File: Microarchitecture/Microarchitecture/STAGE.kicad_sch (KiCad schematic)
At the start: 4 parts

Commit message: Updated timing diagrams, etc, control fsm and verified workings
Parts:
- removed MUX4: ~, symbol Symbols:MUX_BUS
- added MUX2: ~, symbol Symbols:MUX_BUS
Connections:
- net BLAKELEY_MODULE1/A is gone; now on net PREG_RST: REG1. (RST)
- net BLAKELEY_MODULE1/B is gone; now on net DCO: REG8. (RST)
- net BLAKELEY_MODULE1/R: now also MUX1. (MUX[W-1...0])
- net BLAKELEY_MODULE2/R: now also MUX2. (MUX[W-1...0]); no longer MUX1.2 (M1[W-1...0])
- net CMUX_C0: now also MUX1. (MUX[W-1...0])
- net DCI: now also MUX1. (MUX[W-1...0])
- net DPI: now also MUX2. (MUX[W-1...0]); no longer MUX1.1 (M0[W-1...0])
- net DPO: now also REG1. (RST)
- net PMUX_C0: now also MUX2. (MUX[W-1...0]); no longer MUX1.4 (C0)
- new net: MUX2. (MUX[W-1...0]), REG1. (RST)
- new net: MUX1. (MUX[W-1...0]), REG8. (RST)
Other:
- note added: "From rsa_regio"
- note removed: "From upper level"
- moved on the sheet: REG1, REG8

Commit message: Latest changes
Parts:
- renumbered MUX2 to MUX10, MUX1 to MUX9, REG8 to REG16, REG1 to REG17
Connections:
- new net: MUX10. (MUX[W-1...0]), REG17. (RST)
- new net: MUX9. (MUX[W-1...0]), REG16. (RST)
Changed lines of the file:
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@@
 	(wire
 		(pts
-			(xy 302.26 21.59) (xy 302.26 34.29)
+			(xy 307.34 38.1) (xy 307.34 50.8)
 		)
 		(stroke
@@
 	(wire
 		(pts
-			(xy 381 119.38) (xy 396.24 119.38)
+			(xy 374.65 118.11) (xy 389.89 118.11)
 		)
 		(stroke
@@
 	(wire
 		(pts
-			(xy 381 106.68) (xy 396.24 106.68)
+			(xy 374.65 105.41) (xy 389.89 105.41)
 		)
 		(stroke
@@
 	(wire
 		(pts
-			(xy 212.09 115.57) (xy 196.85 115.57)
+			(xy 218.44 115.57) (xy 203.2 115.57)
 		)
 		(stroke
@@
 	(polyline
 		(pts
-			(xy 391.16 95.25) (xy 391.16 127)
+			(xy 384.81 93.98) (xy 384.81 125.73)
 		)
 		(stroke
@@
 	(wire
 		(pts
-			(xy 294.64 21.59) (xy 294.64 34.29)
+			(xy 299.72 38.1) (xy 299.72 50.8)
 		)
 		(stroke
@@
 	(polyline
 		(pts
-			(xy 284.48 26.67) (xy 311.15 26.67)
+			(xy 289.56 43.18) (xy 316.23 43.18)
 		)
 		(stroke
@@
 	(polyline
 		(pts
-			(xy 201.93 93.98) (xy 201.93 125.73)
+			(xy 208.28 93.98) (xy 208.28 125.73)
 		)
 		(stroke
@@
 	(wire
 		(pts
-			(xy 212.09 118.11) (xy 196.85 118.11)
+			(xy 218.44 118.11) (xy 203.2 118.11)
 		)
 		(stroke
@@
 	(wire
 		(pts
-			(xy 381 102.87) (xy 396.24 102.87)
+			(xy 374.65 101.6) (xy 389.89 101.6)
 		)
 		(stroke
@@
 	(wire
 		(pts
-			(xy 212.09 105.41) (xy 196.85 105.41)
+			(xy 218.44 105.41) (xy 203.2 105.41)
 		)
 		(stroke
@@
 	(wire
 		(pts
-			(xy 212.09 101.6) (xy 196.85 101.6)
+			(xy 218.44 101.6) (xy 203.2 101.6)
 		)
 		(stroke
@@
 	(wire
 		(pts
-			(xy 381 116.84) (xy 396.24 116.84)
+			(xy 374.65 115.57) (xy 389.89 115.57)
 		)
 		(stroke
@@
 	)
 	(image
-		(at 144.78 243.84)
-		(scale 0.606573)
+		(at 99.06 242.57)
+		(scale 0.211169)
 		(data "iVBORw0KGgoAAAANSUhEUgAACVEAAAK8CAYAAADsh23GAAAAAXNSR0IArs4c6QAAAARnQU1BAACx"
 			"jwv8YQUAAAAJcEhZcwAAFiUAABYlAUlSJPAAAP+lSURBVHhe7P0PbFT3ne//v20mLNT1jrG/tKak"
@@
 	(text "From rsa_regio"
 		(exclude_from_sim no)
-		(at 282.448 23.368 0)
+		(at 287.528 39.878 0)
 		(effects
 			(font
@@
 	(text "To/From previous stage"
 		(exclude_from_sim no)
-		(at 203.708 91.694 0)
+		(at 210.058 91.694 0)
 		(effects
 			(font
@@
 	(text "To/From next stage"
 		(exclude_from_sim no)
-		(at 390.144 94.234 0)
+		(at 383.794 92.964 0)
 		(effects
 			(font
@@
 	)
 	(label "DCI"
-		(at 212.09 105.41 0)
+		(at 218.44 105.41 0)
 		(fields_autoplaced yes)
 		(effects
@@
 	)
 	(label "ES"
-		(at 302.26 34.29 180)
+		(at 307.34 50.8 180)
 		(fields_autoplaced yes)
 		(effects
@@
 	)
 	(label "IPI"
-		(at 381 116.84 180)
+		(at 374.65 115.57 180)
 		(fields_autoplaced yes)
 		(effects
@@
 	)
 	(label "DPI"
-		(at 212.09 101.6 0)
+		(at 218.44 101.6 0)
 		(fields_autoplaced yes)
 		(effects
@@
 	)
 	(label "DCO"
-		(at 381 106.68 180)
+		(at 374.65 105.41 180)
 		(fields_autoplaced yes)
 		(effects
@@
 	)
 	(label "DPO"
-		(at 381 102.87 180)
+		(at 374.65 101.6 180)
 		(fields_autoplaced yes)
 		(effects
@@
 	)
 	(label "ILO"
-		(at 381 119.38 180)
+		(at 374.65 118.11 180)
 		(fields_autoplaced yes)
 		(effects
@@
 	)
 	(label "ILI"
-		(at 212.09 115.57 0)
+		(at 218.44 115.57 0)
 		(fields_autoplaced yes)
 		(effects
@@
 	)
 	(label "N"
-		(at 294.64 34.29 180)
+		(at 299.72 50.8 180)
 		(fields_autoplaced yes)
 		(effects
@@
 	)
 	(label "IPO"
-		(at 212.09 118.11 0)
+		(at 218.44 118.11 0)
 		(fields_autoplaced yes)
 		(effects
@@
 	(hierarchical_label "ILO"
 		(shape output)
-		(at 396.24 119.38 0)
+		(at 389.89 118.11 0)
 		(fields_autoplaced yes)
 		(effects
@@
 	(hierarchical_label "IPO"
 		(shape output)
-		(at 196.85 118.11 180)
+		(at 203.2 118.11 180)
 		(fields_autoplaced yes)
 		(effects
@@
 	(hierarchical_label "N"
 		(shape input)
-		(at 294.64 21.59 90)
+		(at 299.72 38.1 90)
 		(fields_autoplaced yes)
 		(effects
@@
 	(hierarchical_label "DCO"
 		(shape output)
-		(at 396.24 106.68 0)
+		(at 389.89 105.41 0)
 		(fields_autoplaced yes)
 		(effects
@@
 	(hierarchical_label "IPI"
 		(shape input)
-		(at 396.24 116.84 0)
+		(at 389.89 115.57 0)
 		(fields_autoplaced yes)
 		(effects
@@
 		)
 		(property "Netclass" ""
-			(at 396.24 118.11 0)
+			(at 389.89 116.84 0)
 			(effects
 				(font
@@
 	(hierarchical_label "DCI"
 		(shape input)
-		(at 196.85 105.41 180)
+		(at 203.2 105.41 180)
 		(fields_autoplaced yes)
 		(effects
@@
 	(hierarchical_label "ILI"
 		(shape input)
-		(at 196.85 115.57 180)
+		(at 203.2 115.57 180)
 		(fields_autoplaced yes)
 		(effects
@@
 	(hierarchical_label "ES"
 		(shape input)
-		(at 302.26 21.59 90)
+		(at 307.34 38.1 90)
 		(fields_autoplaced yes)
 		(effects
@@
 	(hierarchical_label "DPI"
 		(shape input)
-		(at 196.85 101.6 180)
+		(at 203.2 101.6 180)
 		(fields_autoplaced yes)
 		(effects
@@
 	(hierarchical_label "DPO"
 		(shape output)
-		(at 396.24 102.87 0)
+		(at 389.89 101.6 0)
 		(fields_autoplaced yes)
 		(effects
@@
 		(on_board yes)
 		(dnp no)
-		(property "Reference" "MUX2"
+		(property "Reference" "MUX10"
 			(at 247.904 137.16 0)
 			(effects
@@
 		)
 		(instances
-			(project ""
-				(path "/7e18b03f-0dd8-4430-9873-65919f4f0c9c/21c2d8ae-34c8-4eeb-a025-0344b2d7e18d/d24df161-92da-4d3c-8ec4-b2b340dd12b4"
-					(reference "MUX2")
+			(project "Microarchitecture"
+				(path "/7e18b03f-0dd8-4430-9873-65919f4f0c9c/21c2d8ae-34c8-4eeb-a025-0344b2d7e18d/2ff9fb5f-e895-4ed8-9926-01fc2395a11b"
+					(reference "MUX10")
+					(unit 1)
+				)
+				(path "/7e18b03f-0dd8-4430-9873-65919f4f0c9c/21c2d8ae-34c8-4eeb-a025-0344b2d7e18d/5c7540d9-7028-48a5-955b-0e835a2154cd"
+					(reference "MUX5")
 					(unit 1)
 				)
@@
 	)
 	(symbol
-		(lib_name "Symbols:REG")
 		(lib_id "Symbols:REG")
 		(at 313.69 66.04 0)
@@
 		(on_board yes)
 		(dnp no)
-		(property "Reference" "REG8"
+		(property "Reference" "REG16"
 			(at 319.786 57.658 0)
 			(effects
@@
 		(instances
 			(project "Microarchitecture"
+				(path "/7e18b03f-0dd8-4430-9873-65919f4f0c9c/21c2d8ae-34c8-4eeb-a025-0344b2d7e18d/2ff9fb5f-e895-4ed8-9926-01fc2395a11b"
+					(reference "REG16")
+					(unit 1)
+				)
+				(path "/7e18b03f-0dd8-4430-9873-65919f4f0c9c/21c2d8ae-34c8-4eeb-a025-0344b2d7e18d/5c7540d9-7028-48a5-955b-0e835a2154cd"
+					(reference "REG4")
+					(unit 1)
+				)
 				(path "/7e18b03f-0dd8-4430-9873-65919f4f0c9c/21c2d8ae-34c8-4eeb-a025-0344b2d7e18d/d24df161-92da-4d3c-8ec4-b2b340dd12b4"
 					(reference "REG8")
@@
 	)
 	(symbol
-		(lib_name "Symbols:REG")
 		(lib_id "Symbols:REG")
 		(at 313.69 152.4 0)
@@
 		(on_board yes)
 		(dnp no)
-		(property "Reference" "REG1"
+		(property "Reference" "REG17"
 			(at 319.786 144.018 0)
 			(effects
@@
 		(instances
 			(project "Microarchitecture"
+				(path "/7e18b03f-0dd8-4430-9873-65919f4f0c9c/21c2d8ae-34c8-4eeb-a025-0344b2d7e18d/2ff9fb5f-e895-4ed8-9926-01fc2395a11b"
+					(reference "REG17")
+					(unit 1)
+				)
+				(path "/7e18b03f-0dd8-4430-9873-65919f4f0c9c/21c2d8ae-34c8-4eeb-a025-0344b2d7e18d/5c7540d9-7028-48a5-955b-0e835a2154cd"
+					(reference "REG6")
+					(unit 1)
+				)
 				(path "/7e18b03f-0dd8-4430-9873-65919f4f0c9c/21c2d8ae-34c8-4eeb-a025-0344b2d7e18d/d24df161-92da-4d3c-8ec4-b2b340dd12b4"
 					(reference "REG1")
@@
 		(on_board yes)
 		(dnp no)
-		(property "Reference" "MUX1"
+		(property "Reference" "MUX9"
 			(at 247.904 50.8 0)
 			(effects
@@
 		(instances
 			(project "Microarchitecture"
+				(path "/7e18b03f-0dd8-4430-9873-65919f4f0c9c/21c2d8ae-34c8-4eeb-a025-0344b2d7e18d/2ff9fb5f-e895-4ed8-9926-01fc2395a11b"
+					(reference "MUX9")
+					(unit 1)
+				)
+				(path "/7e18b03f-0dd8-4430-9873-65919f4f0c9c/21c2d8ae-34c8-4eeb-a025-0344b2d7e18d/5c7540d9-7028-48a5-955b-0e835a2154cd"
+					(reference "MUX4")
+					(unit 1)
+				)
 				(path "/7e18b03f-0dd8-4430-9873-65919f4f0c9c/21c2d8ae-34c8-4eeb-a025-0344b2d7e18d/d24df161-92da-4d3c-8ec4-b2b340dd12b4"
 					(reference "MUX1")
@@
 					(page "6")
 				)
+				(path "/7e18b03f-0dd8-4430-9873-65919f4f0c9c/21c2d8ae-34c8-4eeb-a025-0344b2d7e18d/5c7540d9-7028-48a5-955b-0e835a2154cd"
+					(page "10")
+				)
+				(path "/7e18b03f-0dd8-4430-9873-65919f4f0c9c/21c2d8ae-34c8-4eeb-a025-0344b2d7e18d/2ff9fb5f-e895-4ed8-9926-01fc2395a11b"
+					(page "13")
+				)
 			)
 		)
@@
 					(page "5")
 				)
+				(path "/7e18b03f-0dd8-4430-9873-65919f4f0c9c/21c2d8ae-34c8-4eeb-a025-0344b2d7e18d/5c7540d9-7028-48a5-955b-0e835a2154cd"
+					(page "11")
+				)
+				(path "/7e18b03f-0dd8-4430-9873-65919f4f0c9c/21c2d8ae-34c8-4eeb-a025-0344b2d7e18d/2ff9fb5f-e895-4ed8-9926-01fc2395a11b"
+					(page "14")
+				)
 			)

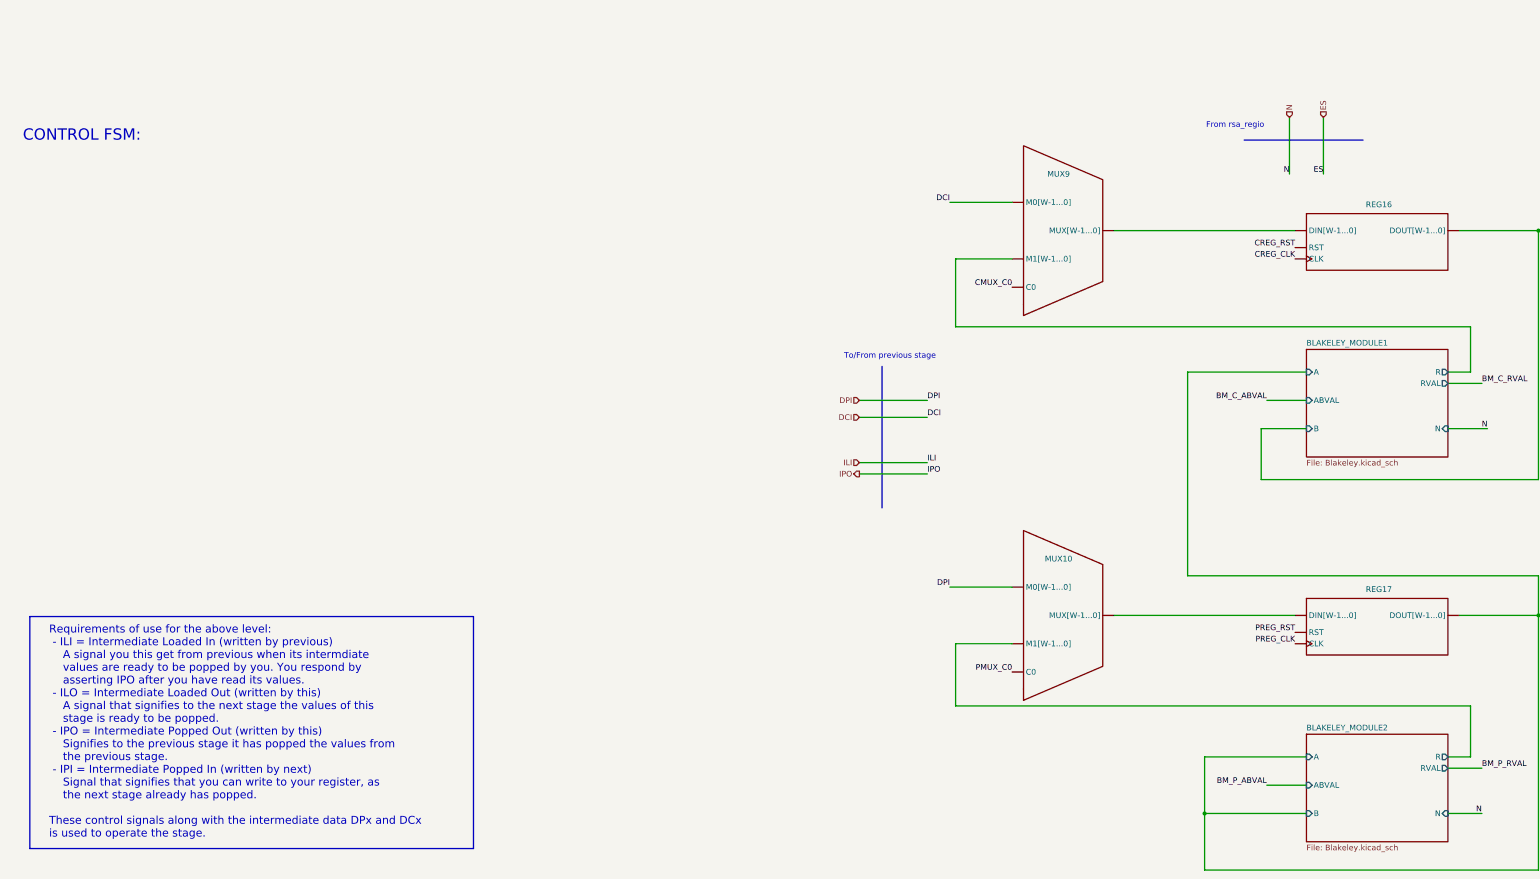
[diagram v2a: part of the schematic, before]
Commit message: Added rev2 BLAKELEY_MODULE
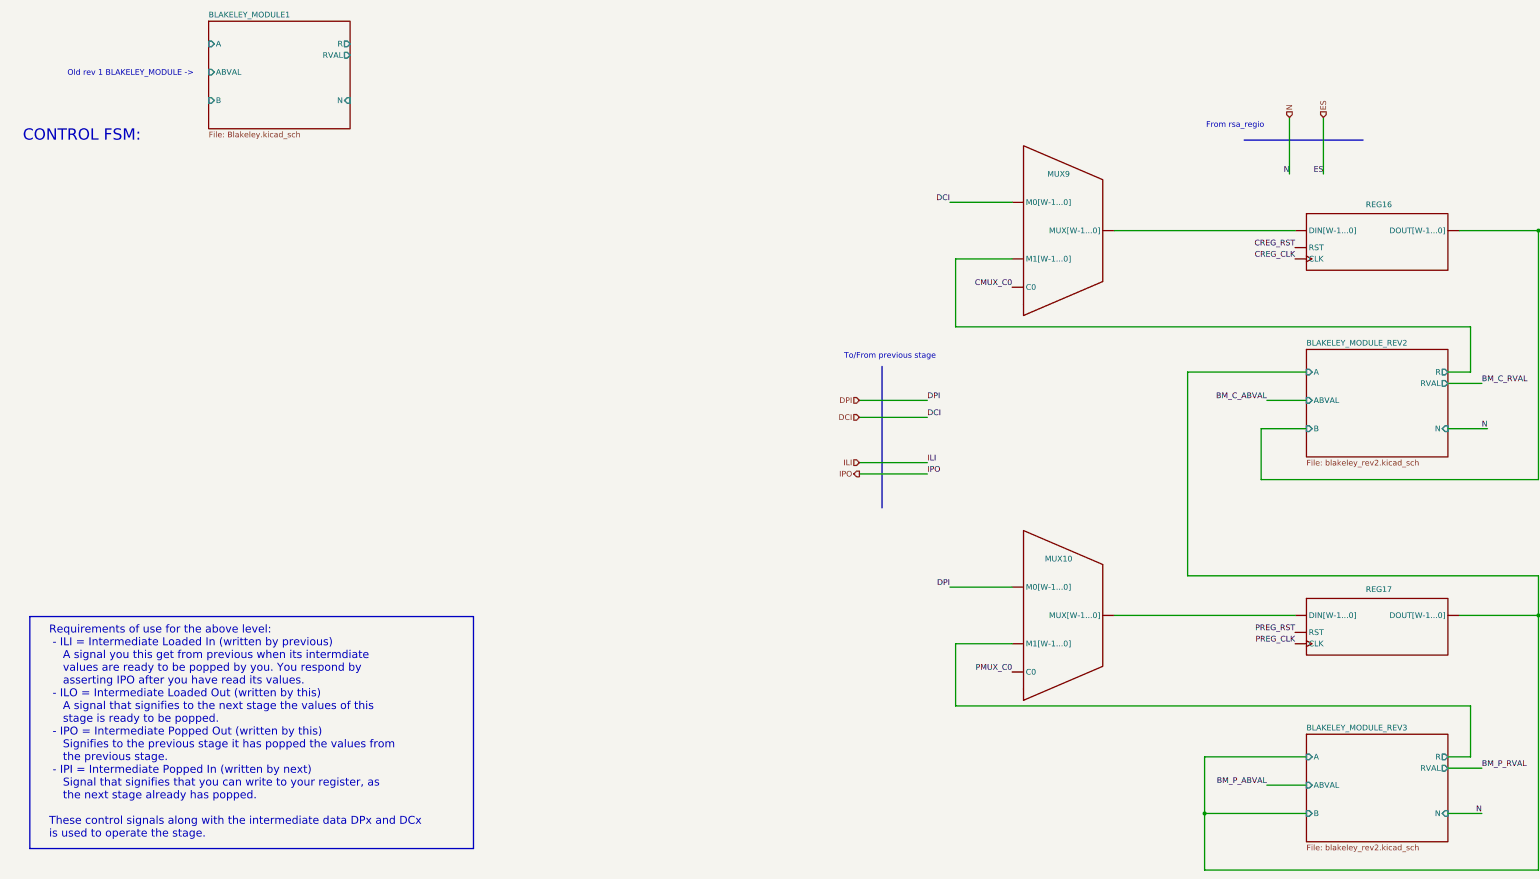
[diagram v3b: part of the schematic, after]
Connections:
- net BLAKELEY_MODULE2/R is gone; now on net PMUX_C0: MUX10. (MUX[W-1...0])
- net BLAKELEY_MODULE1/R: no longer MUX9. (MUX[W-1...0])
- new net: MUX10. (MUX[W-1...0]), REG17. (RST)
- new net: MUX9. (MUX[W-1...0]), REG16. (RST)
- new net BLAKELEY_MODULE_REV2/R: MUX9. (MUX[W-1...0])
- new net BLAKELEY_MODULE_REV3/R: MUX10. (MUX[W-1...0])
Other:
- removed sheet BLAKELEY_MODULE2
- added sheet BLAKELEY_MODULE_REV2 (blakeley_rev2.kicad_sch)
- added sheet BLAKELEY_MODULE_REV3 (blakeley_rev2.kicad_sch)
- note added: "Old rev 1 BLAKELEY_MODULE ->"
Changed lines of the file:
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@@
 	)
 	(image
-		(at 99.06 242.57)
-		(scale 0.211169)
+		(at 143.51 241.3)
+		(scale 0.58991)
 		(data "iVBORw0KGgoAAAANSUhEUgAACVEAAAK8CAYAAADsh23GAAAAAXNSR0IArs4c6QAAAARnQU1BAACx"
 			"jwv8YQUAAAAJcEhZcwAAFiUAABYlAUlSJPAAAP+lSURBVHhe7P0PbFT3ne//v20mLNT1jrG/tKak"
@@
 		)
 	)
+	(text "Old rev 1 BLAKELEY_MODULE ->"
+		(exclude_from_sim no)
+		(at 39.624 28.194 0)
+		(effects
+			(font
+				(size 1.27 1.27)
+			)
+		)
+	)
 	(text "From rsa_regio"
 		(exclude_from_sim no)
@@
 	)
 	(sheet
-		(at 303.53 90.17)
+		(at 57.15 16.51)
 		(size 31.75 24.13)
 		(fields_autoplaced yes)
@@
 		)
 		(property "Sheetname" "BLAKELEY_MODULE1"
-			(at 303.53 89.4584 0)
+			(at 57.15 15.7984 0)
 			(effects
 				(font
@@
 		)
 		(property "Sheetfile" "Blakeley.kicad_sch"
-			(at 303.53 114.8846 0)
+			(at 57.15 41.2246 0)
 			(effects
 				(font
@@
 		)
 		(pin "N" input
-			(at 335.28 107.95 0)
+			(at 88.9 34.29 0)
 			(effects
 				(font
@@
 		)
 		(pin "B" input
-			(at 303.53 107.95 180)
+			(at 57.15 34.29 180)
 			(effects
 				(font
@@
 		)
 		(pin "A" input
-			(at 303.53 95.25 180)
+			(at 57.15 21.59 180)
 			(effects
 				(font
@@
 		)
 		(pin "R" output
-			(at 335.28 95.25 0)
+			(at 88.9 21.59 0)
 			(effects
 				(font
@@
 		)
 		(pin "RVAL" output
-			(at 335.28 97.79 0)
+			(at 88.9 24.13 0)
 			(effects
 				(font
@@
 		)
 		(pin "ABVAL" input
-			(at 303.53 101.6 180)
+			(at 57.15 27.94 180)
 			(effects
 				(font
@@
 	)
 	(sheet
-		(at 303.53 176.53)
+		(at 303.53 90.17)
 		(size 31.75 24.13)
 		(fields_autoplaced yes)
@@
 			(color 0 0 0 0.0000)
 		)
-		(property "Sheetname" "BLAKELEY_MODULE2"
+		(property "Sheetname" "BLAKELEY_MODULE_REV2"
+			(at 303.53 89.4584 0)
+			(effects
+				(font
+					(size 1.27 1.27)
+				)
+				(justify left bottom)
+			)
+		)
+		(property "Sheetfile" "blakeley_rev2.kicad_sch"
+			(at 303.53 114.8846 0)
+			(effects
+				(font
+					(size 1.27 1.27)
+				)
+				(justify left top)
+			)
+		)
+		(pin "A" input
+			(at 303.53 95.25 180)
+			(effects
+				(font
+					(size 1.27 1.27)
+				)
+				(justify left)
+			)
+		)
+		(pin "B" input
+			(at 303.53 107.95 180)
+			(effects
+				(font
+					(size 1.27 1.27)
+				)
+				(justify left)
+			)
+		)
+		(pin "ABVAL" input
+			(at 303.53 101.6 180)
+			(effects
+				(font
+					(size 1.27 1.27)
+				)
+				(justify left)
+			)
+		)
+		(pin "N" input
+			(at 335.28 107.95 0)
+			(effects
+				(font
+					(size 1.27 1.27)
+				)
+				(justify right)
+			)
+		)
+		(pin "R" output
+			(at 335.28 95.25 0)
+			(effects
+				(font
+					(size 1.27 1.27)
+				)
+				(justify right)
+			)
+		)
+		(pin "RVAL" output
+			(at 335.28 97.79 0)
+			(effects
+				(font
+					(size 1.27 1.27)
+				)
+				(justify right)
+			)
+		)
+		(instances
+			(project "Microarchitecture"
+				(path "/7e18b03f-0dd8-4430-9873-65919f4f0c9c/21c2d8ae-34c8-4eeb-a025-0344b2d7e18d/d24df161-92da-4d3c-8ec4-b2b340dd12b4"
+					(page "15")
+				)
+			)
+		)
+	)
+	(sheet
+		(at 303.53 176.53)
+		(size 31.75 24.13)
+		(fields_autoplaced yes)
+		(stroke
+			(width 0.1524)
+			(type solid)
+		)
+		(fill
+			(color 0 0 0 0.0000)
+		)
+		(property "Sheetname" "BLAKELEY_MODULE_REV3"
 			(at 303.53 175.8184 0)
 			(effects
@@
 			)
 		)
-		(property "Sheetfile" "Blakeley.kicad_sch"
+		(property "Sheetfile" "blakeley_rev2.kicad_sch"
 			(at 303.53 201.2446 0)
 			(effects
@@
 				)
 				(justify left top)
+			)
+		)
+		(pin "A" input
+			(at 303.53 181.61 180)
+			(effects
+				(font
+					(size 1.27 1.27)
+				)
+				(justify left)
+			)
+		)
+		(pin "B" input
+			(at 303.53 194.31 180)
+			(effects
+				(font
+					(size 1.27 1.27)
+				)
+				(justify left)
+			)
+		)
+		(pin "ABVAL" input
+			(at 303.53 187.96 180)
+			(effects
+				(font
+					(size 1.27 1.27)
+				)
+				(justify left)
 			)
 		)
@@
 			)
 		)
-		(pin "B" input
-			(at 303.53 194.31 180)
-			(effects
-				(font
-					(size 1.27 1.27)
-				)
-				(justify left)
-			)
-		)
-		(pin "A" input
-			(at 303.53 181.61 180)
-			(effects
-				(font
-					(size 1.27 1.27)
-				)
-				(justify left)
-			)
-		)
 		(pin "R" output
 			(at 335.28 181.61 0)
@@
 			)
 		)
-		(pin "ABVAL" input
-			(at 303.53 187.96 180)
-			(effects
-				(font
-					(size 1.27 1.27)
-				)
-				(justify left)
-			)
-		)

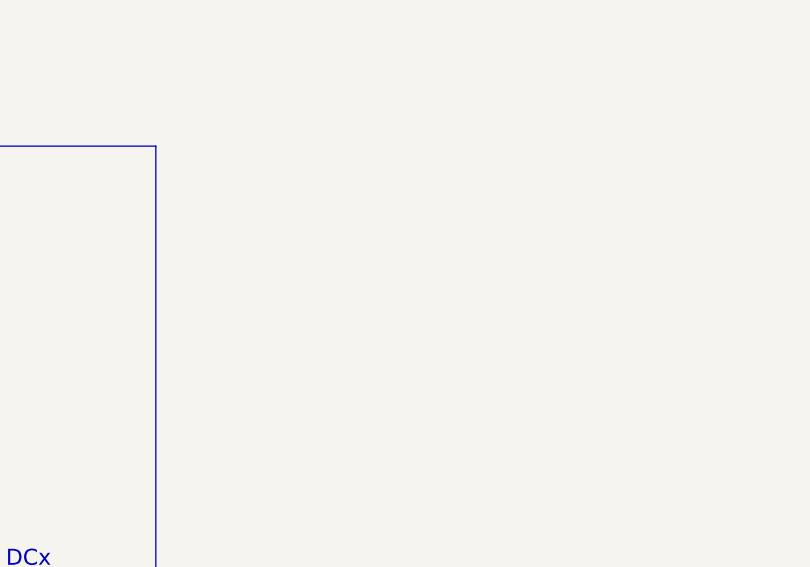
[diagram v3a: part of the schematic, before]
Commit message: Removed debugging layouts
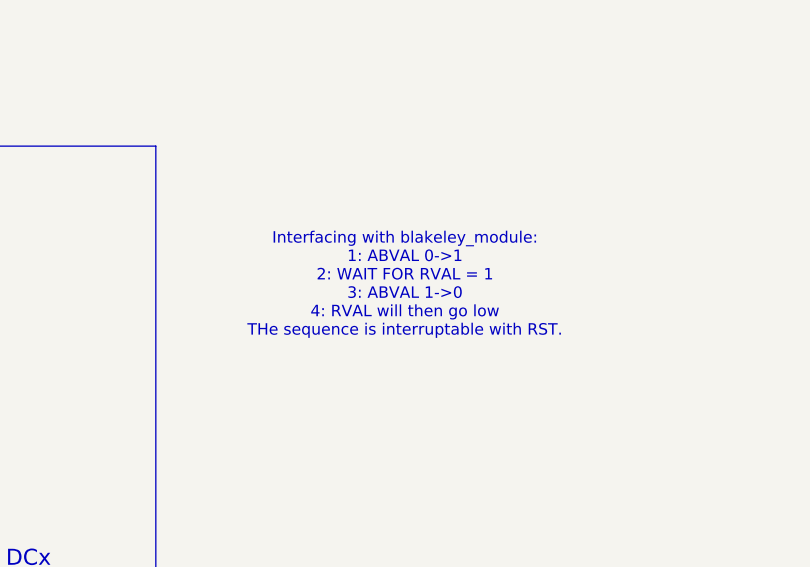
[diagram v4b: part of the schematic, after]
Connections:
- new net: MUX10. (MUX[W-1...0]), REG17. (RST)
- new net: MUX9. (MUX[W-1...0]), REG16. (RST)
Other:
- note added: "Interfacing with blakeley_module: 1: ABVAL 0->1 2: WAIT FOR RVAL = 1 3: ABVAL 1->0 4: RVAL will then go low THe sequence is interruptable with RST."
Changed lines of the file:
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@@
+		)
+	)
+	(text "Interfacing with blakeley_module:\n1: ABVAL 0->1\n2: WAIT FOR RVAL = 1\n3: ABVAL 1->0\n4: RVAL will then go low\nTHe sequence is interruptable with RST."
+		(exclude_from_sim no)
+		(at 144.272 165.608 0)
+		(effects
+			(font
+				(size 1.27 1.27)
+			)
 		)
 	)
